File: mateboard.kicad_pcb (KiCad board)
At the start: 6 copper layers, 70 x 50 mm, 178 parts, among them IC1 OSD335x, IC2 SN74LVC2G241DCUR, IC3 NAND_4GB, IC4 WL1835MODGBMOCT, J1 IO1, J10 TEST_1P, J11 TEST_1P, J12 ANT2, J13 TEST_1P, J14 TEST_1P, J15 VDDS_PLL, J16 VDDS_DDR, J17 VDD_MPU, J18 VDD_CORE, J2 IO2, J3 GS2, J4 ANT2, J5 TEST_1P, J6 TEST_1P, J7 TEST_1P, J8 TEST_1P, J9 TEST_1P, Q1 BSS138, Q2 BSS138, U1 AP2112K-3.3TRG1, U10 TXS0108, U11 TXS0108, U2 AP2112K-1.8TRG1, U3 TL1963A-33DCQR, U4 24LC32AT-I, U5 TPS2065CDGN, U6 TPD4S012, U7 TPD4S012, U8 SN74LVC1G06DCK, U9 74LVC1G07DCK, X1 NZ2520SB-32.768KHZ-NSA3534C, Y1 24MHz, Y2 32.768kHz

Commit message: footprint check
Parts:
- U5: footprint Housings_SSOP:VSSOP-8_2.3x2mm_Pitch0.5mm -> Housings_SSOP:MSOP-8-1EP_3x3mm_Pitch0.65mm
- moved J11 13.5 mm to (65.0, 66.0)
- moved J8 11.5 mm to (63.0, 63.0)
- moved J10 10.0 mm to (63.0, 65.0)
- moved J2 7.67 mm to (54.0, 65.0)
- moved J1 6.03 mm to (116.0, 65.0)
- moved U5 4.51 mm to (117.5, 53.5)
- moved R6 4.29 mm to (115.0, 55.0)
- moved L2 4.00 mm to (118.4, 58.1)
- moved L3 4.00 mm to (116.4, 58.1)
- moved R8 3.98 mm to (115.0, 52.0), turned to 270 degrees
- moved C13 3.84 mm to (116.0, 49.2), turned to 180 degrees
- moved C28 0.60 mm to (89.8, 56.0)
- moved C20 0.50 mm to (101.3, 54.0)
- moved C22 0.50 mm to (99.8, 46.9)
- moved C23 0.50 mm to (83.0, 44.9)
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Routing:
- net VDD_3V3B: track 0.00 -> 7.56 mm, vias 0 -> 2

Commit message: wip routing
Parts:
- moved L2 3.17 mm to (118.4, 61.3)
- moved L3 3.17 mm to (116.4, 61.3)
- moved J2 3.00 mm to (54.0, 62.0)
- moved R23 1.20 mm to (113.2, 64.4)
- moved R25 1.20 mm to (113.2, 65.6)
- moved C10 0.53 mm to (65.5, 44.3)
- moved C3 0.50 mm to (104.5, 55.7)
- moved C9 0.50 mm to (100.9, 55.7)
- moved IC1 0.20 mm to (98.3, 70.3)
- moved R30 0.10 mm to (107.6, 85.1)
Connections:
- IC3 pad A2: (no net) -> /System-eMMC-GPIO/MMC1_DAT4
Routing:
- net VDD_3V3_WIFI: track 0.00 -> 87.7 mm, vias 0 -> 6
- net VDD_5V: track 0.00 -> 62.4 mm, vias 0 -> 7
- net VDD_3V3A: track 0.00 -> 37.4 mm, vias 0 -> 4
- net USB_DC: track 0.00 -> 26.7 mm, vias 0 -> 2
- net Net-(C6-Pad1): track 0.00 -> 19.3 mm
- net /LCD_DATA15: track 0.00 -> 15.5 mm, vias 0 -> 2
- net /VBAT: track 0.00 -> 14.6 mm, vias 0 -> 3
- net VDD_ADC: track 0.00 -> 13.0 mm, vias 0 -> 3
- net GNDD: track 0.00 -> 12.9 mm, vias 0 -> 8
- net /LCD_DATA3: track 0.00 -> 12.5 mm, vias 0 -> 2
- net /LCD_DATA2: track 0.00 -> 11.9 mm, vias 0 -> 2
- net /LCD_DATA14: track 0.00 -> 10.5 mm
- net Net-(D1-Pad1): track 0.00 -> 9.60 mm
- net /LCD_DATA11: track 0.00 -> 9.51 mm, vias 0 -> 2
- net SYS_5V: track 0.00 -> 7.48 mm
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
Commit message: wip routing
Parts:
- moved R39 15.6 mm to (95.1, 54.4), turned to 180 degrees
- moved R40 10.7 mm to (93.2, 54.4), turned to 180 degrees
- moved R38 5.22 mm to (83.5, 47.5)
- moved C26 3.00 mm to (99.5, 48.6)
- moved C22 2.90 mm to (99.7, 49.8)
- moved R36 2.20 mm to (99.2, 46.0)
- moved R37 2.20 mm to (99.2, 47.2)
- moved R44 1.20 mm to (83.5, 48.7)
- moved R45 1.20 mm to (83.5, 49.9)
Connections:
- IC3 pad A8: (no net) -> /System-eMMC-GPIO/MMC1_DAT7
- IC3 pad B7: (no net) -> /System-eMMC-GPIO/MMC1_DAT7
- IC3 pad C1: (no net) -> Net-(C25-Pad1)
- IC3 pad C3: (no net) -> /System-eMMC-GPIO/MMC1_DAT5
- IC3 pad C5: (no net) -> /System-eMMC-GPIO/MMC1_DAT6
- IC3 pad D1: (no net) -> /System-eMMC-GPIO/MMC1_DAT5
- IC3 pad D2: (no net) -> /System-eMMC-GPIO/MMC1_DAT5
- IC3 pad D3: (no net) -> GNDD
- IC3 pad D4: (no net) -> /System-eMMC-GPIO/MMC1_DAT6
- IC3 pad E1: (no net) -> GNDD
- IC3 pad E2: (no net) -> GNDD
- IC3 pad E3: (no net) -> /System-eMMC-GPIO/MMC1_DAT6
- IC3 pad F2: (no net) -> /System-eMMC-GPIO/MMC1_DAT6
- IC3 pad G1: (no net) -> /System-eMMC-GPIO/MMC1_DAT6
- IC3 pad M7: (no net) -> /System-eMMC-GPIO/MMC1_CLK
- IC3 pad N6: (no net) -> /System-eMMC-GPIO/MMC1_CMD
- IC3 pad N7: (no net) -> /System-eMMC-GPIO/MMC1_CMD
- IC3 pad N8: (no net) -> /System-eMMC-GPIO/MMC1_CLK
- IC3 pad P2: (no net) -> GNDD
- IC3 pad P8: (no net) -> /System-eMMC-GPIO/MMC1_CMD
- IC3 pad P9: (no net) -> /System-eMMC-GPIO/MMC1_CLK
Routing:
- net VDD_3V3B: track 11.5 -> 32.6 mm, vias 2 -> 3
- net USB_DC: track 26.7 -> 47.1 mm, vias 2 -> 3
- net GNDD: track 12.9 -> 29.2 mm, vias 8 -> 12
- net /System-eMMC-GPIO/eMMC_RSTn: track 0.00 -> 10.7 mm, vias 0 -> 2
- net /System-eMMC-GPIO/MMC1_DAT6: track 0.00 -> 8.83 mm
- net VDD_5V: track 62.4 -> 71.0 mm
- net /System-eMMC-GPIO/MMC1_DAT5: track 0.00 -> 7.50 mm
- net /System-eMMC-GPIO/MMC1_CLK: track 0.00 -> 6.38 mm
- net /System-eMMC-GPIO/MMC1_CMD: track 0.00 -> 6.09 mm
- net Net-(C25-Pad1): track 0.00 -> 5.54 mm
- net /System-eMMC-GPIO/MMC1_DAT7: track 0.00 -> 5.51 mm
- net SYS_5V: track 7.48 -> 12.1 mm
- net /System-eMMC-GPIO/MMC1_DAT1: track 0.00 -> 4.47 mm
- net /System-eMMC-GPIO/MMC1_DAT2: track 0.00 -> 4.41 mm
- net /USB-UART-WL-BT-GPIO/USB1_PWR: track 7.04 -> 10.7 mm
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
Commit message: wip routing
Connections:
- IC3 pad A9: (no net) -> VDD_3V3B
- IC3 pad B8: (no net) -> VDD_3V3B
- IC3 pad C7: (no net) -> VDD_3V3B
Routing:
- net SYS_5V: track 12.1 -> 63.2 mm, vias 0 -> 6
- net /System-eMMC-GPIO/MMC1_DAT2: track 4.41 -> 29.7 mm, vias 0 -> 2
- net /System-eMMC-GPIO/MMC1_DAT7: track 5.51 -> 30.8 mm, vias 0 -> 2
- net GNDD: track 29.2 -> 54.1 mm, vias 12 -> 17
- net /System-eMMC-GPIO/MMC1_DAT0: track 4.76 -> 27.4 mm, vias 0 -> 2
- net VDD_3V3B: track 32.6 -> 54.7 mm
- net /System-eMMC-GPIO/MMC1_DAT1: track 4.47 -> 25.7 mm, vias 0 -> 2
- net /System-eMMC-GPIO/MMC1_DAT3: track 6.04 -> 26.6 mm, vias 0 -> 2
- net /System-eMMC-GPIO/MMC1_DAT4: track 5.75 -> 26.0 mm, vias 0 -> 2
- net /System-eMMC-GPIO/MMC1_DAT5: track 7.50 -> 23.5 mm, vias 0 -> 2
- net Net-(C16-Pad2): track 0.00 -> 14.6 mm, vias 0 -> 2
- net /System-eMMC-GPIO/MMC1_DAT6: track 8.83 -> 22.6 mm, vias 0 -> 2
- net GNDA: track 0.00 -> 13.3 mm, vias 0 -> 3
- net Net-(IC1-PadP15): track 0.00 -> 12.3 mm, vias 0 -> 2
- net Net-(IC1-PadB12): track 0.00 -> 10.6 mm, vias 0 -> 2
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
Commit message: wip routing wifi
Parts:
- moved R34 10.5 mm to (113.2, 75.2)
- moved R50 3.70 mm to (55.5, 53.3)
- moved J16 2.77 mm to (107.3, 74.9)
- moved J15 2.67 mm to (107.3, 79.2)
- moved R52 1.14 mm to (56.7, 53.4)
- moved R53 1.14 mm to (57.9, 53.4)
- moved R54 1.14 mm to (59.1, 53.4)
- moved J17 0.45 mm to (97.0, 76.7)
- moved AE1 0.34 mm to (51.4, 73.7)
- moved C36 0.12 mm to (51.4, 71.9)
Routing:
- net GNDD: track 54.1 -> 216.6 mm, vias 17 -> 59
- net VDD_3V3B: track 54.7 -> 199.7 mm, vias 3 -> 15
- net GNDA: track 13.3 -> 73.4 mm, vias 3 -> 4
- net /USB-UART-WL-BT-GPIO/USB1_DRVVBUS: track 1.65 -> 46.2 mm, vias 0 -> 2
- net SYS_5V: track 63.2 -> 103.4 mm, vias 6 -> 7
- net /System-eMMC-GPIO/MMC1_CLK: track 6.38 -> 43.3 mm, vias 0 -> 2
- net /Wi-Fi BLE/WL_IRQ: track 0.00 -> 35.9 mm, vias 0 -> 2
- net /System-eMMC-GPIO/MMC1_CMD: track 6.09 -> 40.3 mm, vias 0 -> 2
- net /Power Management/LDO_PGOOD: track 0.00 -> 33.5 mm, vias 0 -> 2
- net VDD_1V8_WIFI: track 0.00 -> 26.6 mm
- net VDD_3V3A: track 38.8 -> 62.5 mm, vias 4 -> 6
- net Net-(IC1-PadC6): track 0.00 -> 20.5 mm, vias 0 -> 2
- net /Power Management/PMIC_PGOOD: track 0.00 -> 20.3 mm, vias 0 -> 2
- net /Wi-Fi BLE/WL_SDIO_D3: track 0.00 -> 18.8 mm, vias 0 -> 2
- net /USB-UART-WL-BT-GPIO/UART0_RXD.CPU: track 0.00 -> 17.3 mm, vias 0 -> 2
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- added copper zone on Ground.Cu, net GNDD

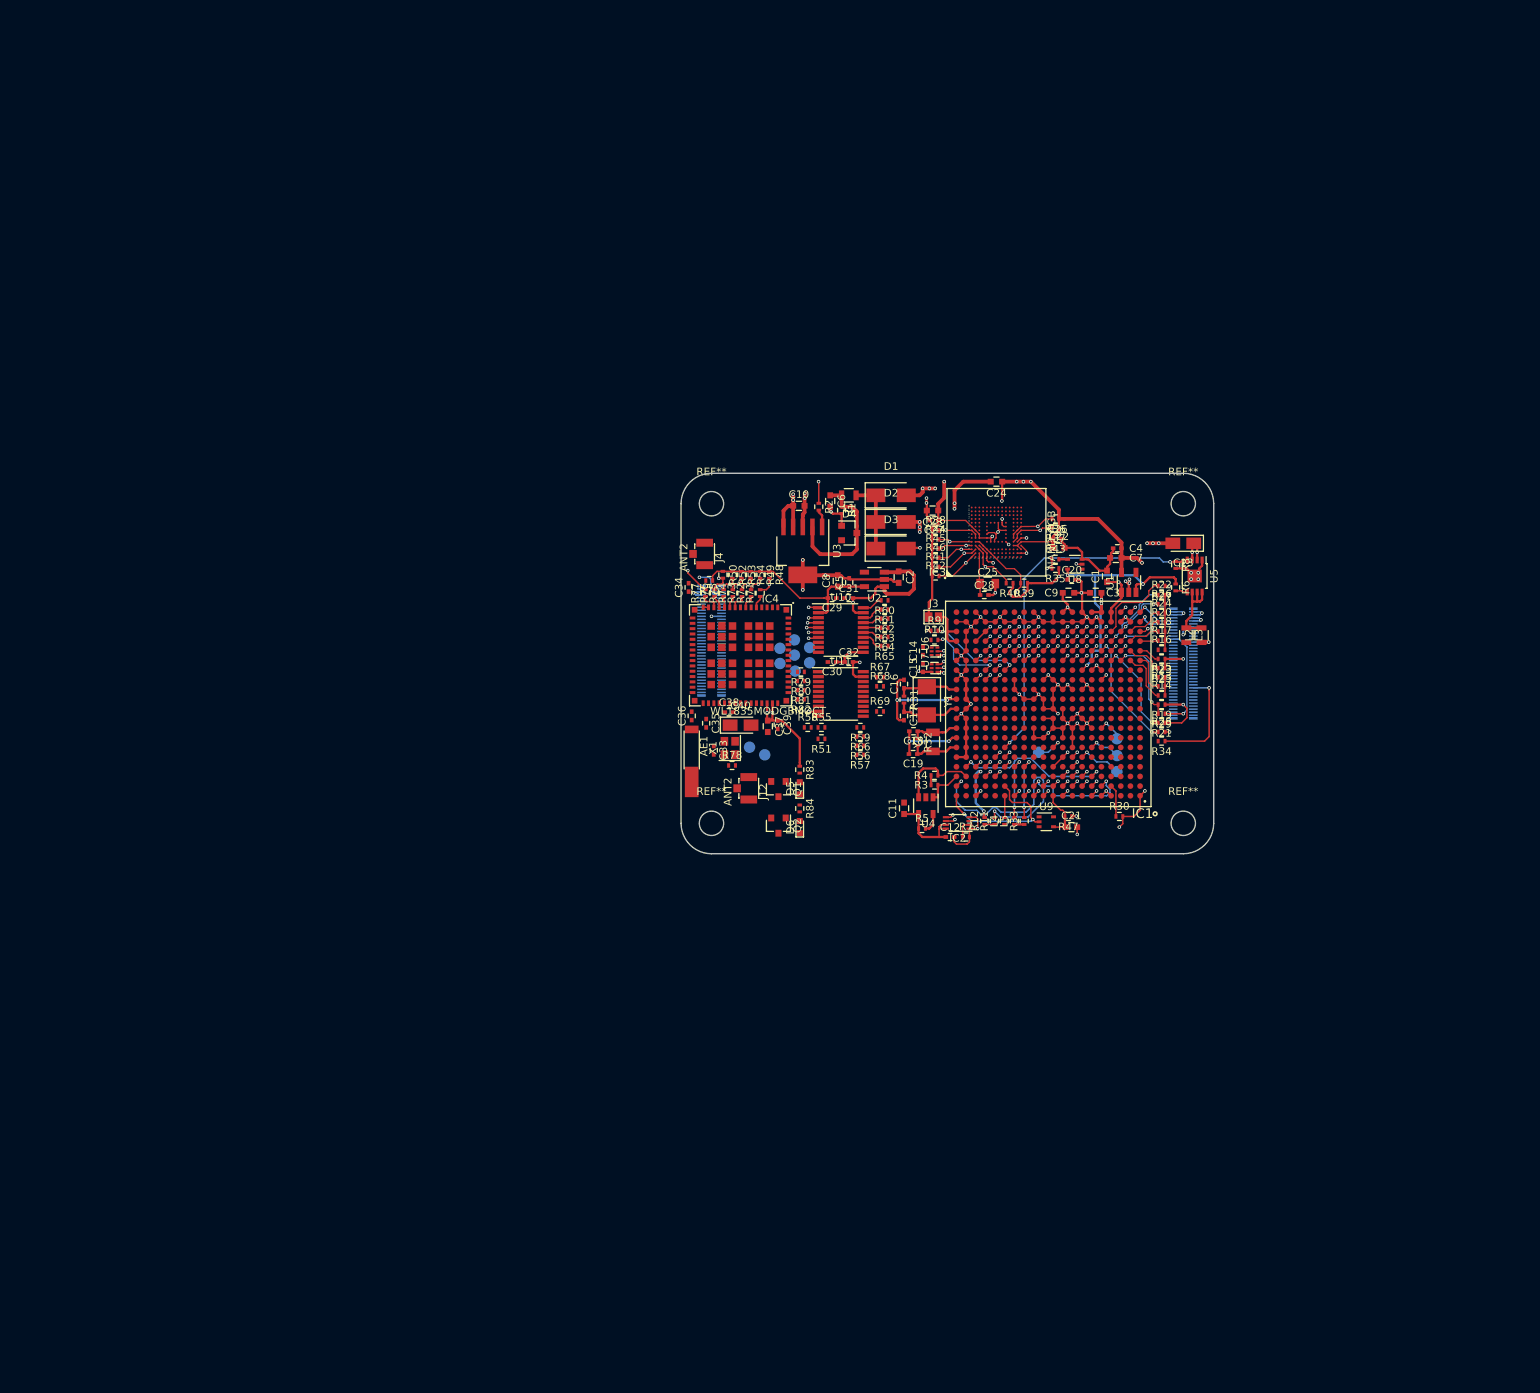
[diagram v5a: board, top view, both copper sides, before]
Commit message: connector pinout rearrangement
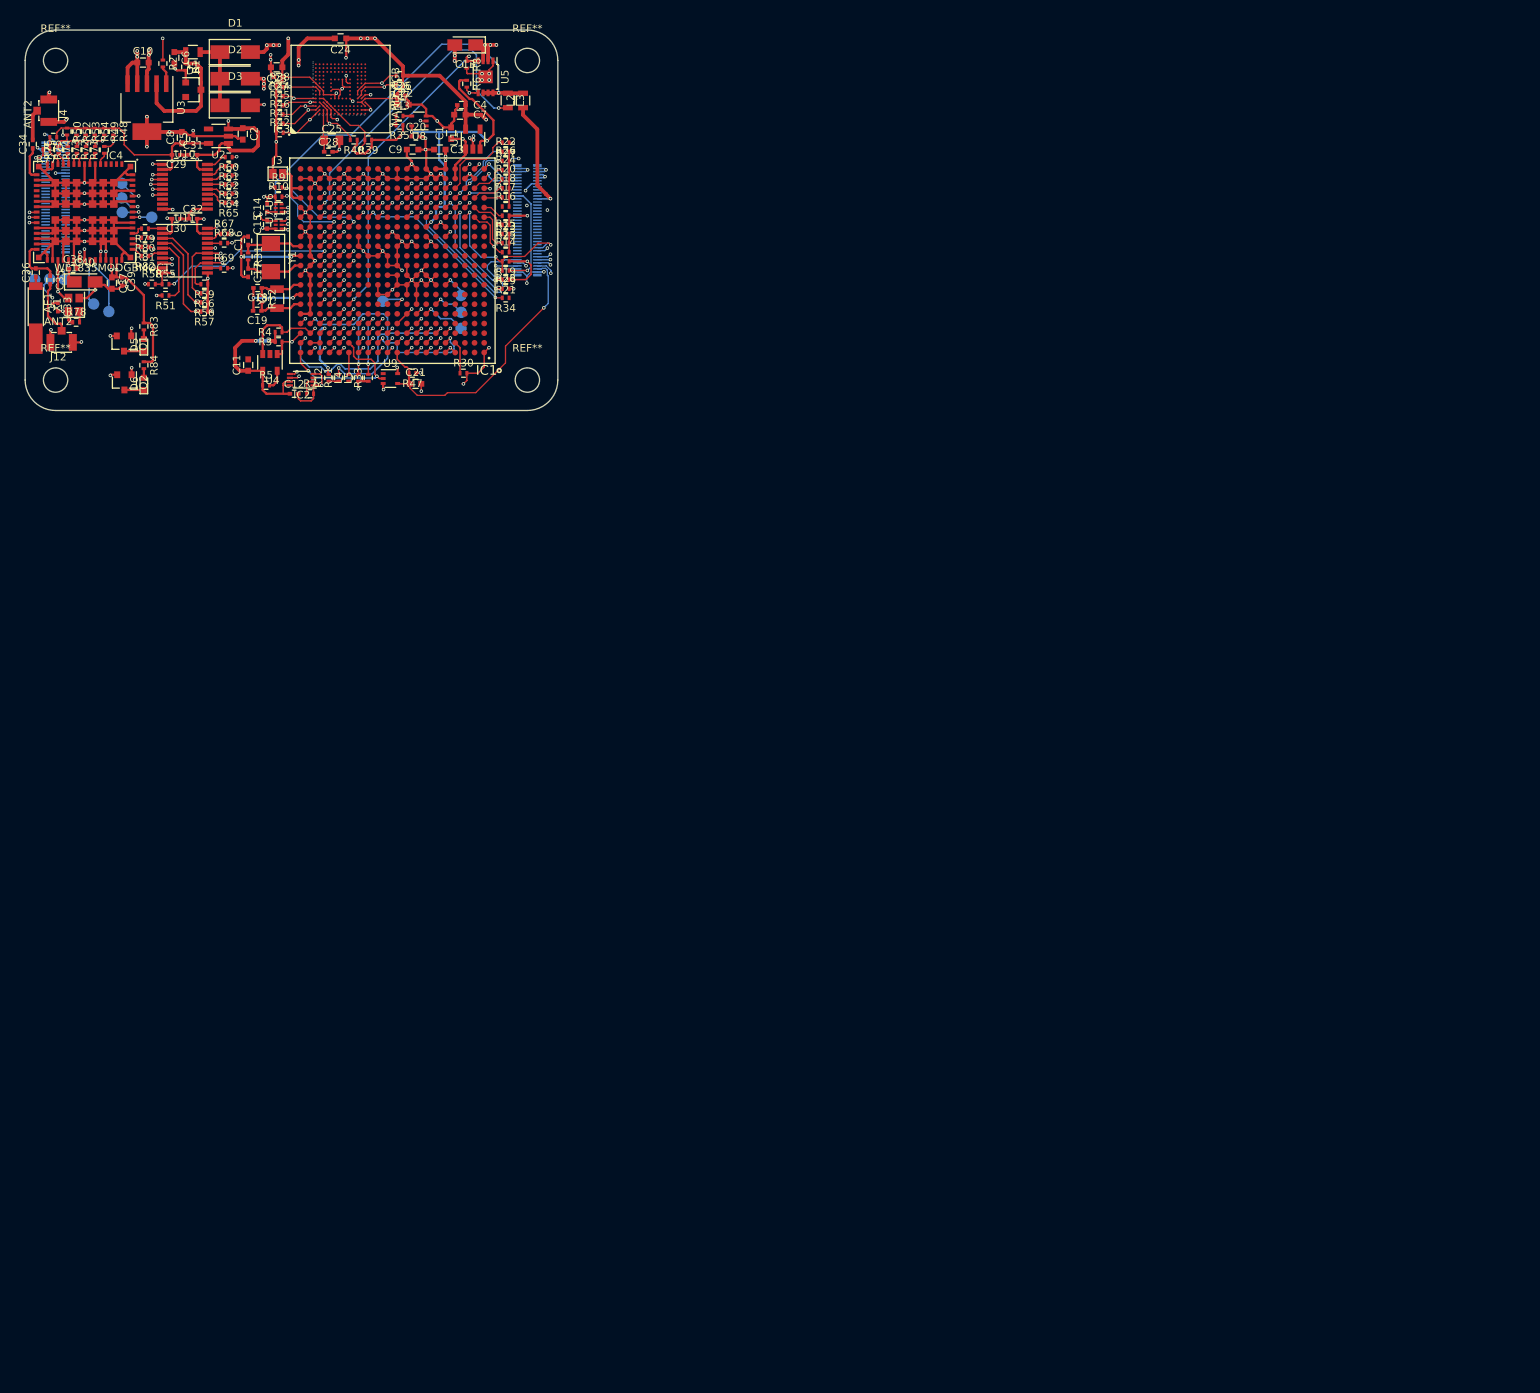
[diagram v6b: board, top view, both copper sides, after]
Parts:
- moved C13 114.9 mm to (21.6, -16.3)
- moved R6 114.3 mm to (21.8, -11.2)
- moved R8 114.0 mm to (21.8, -13.7)
- moved U5 114.0 mm to (24.3, -12.1)
- moved L2 113.5 mm to (29.2, -8.99)
- moved L3 113.5 mm to (27.2, -8.99)
- moved J8 109.3 mm to (-34.9, 14.5)
- moved J11 109.0 mm to (-31.1, 14.5)
- moved J10 108.4 mm to (-33.0, 14.5)
- moved J6 108.0 mm to (-23.5, 3.81)
- moved J12 107.6 mm to (-31.4, 22.8), turned to 180 degrees
- moved J5 106.8 mm to (-23.5, 1.91)
- moved J7 105.8 mm to (-23.4, 5.71)
- moved J17 104.6 mm to (10.8, 17.4)
- moved R77 104.4 mm to (-33.4, -2.60), turned to 180 degrees
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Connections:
- D4 pad 2: (no net) -> Net-(D4-Pad2)
- IC1 pad A2: (no net) -> Net-(IC1-PadA2)
- IC1 pad A3: (no net) -> Net-(IC1-PadA3)
- IC1 pad B1: (no net) -> Net-(IC1-PadB1)
- IC1 pad B2: (no net) -> Net-(IC1-PadB2)
- IC1 pad B3: (no net) -> Net-(IC1-PadB3)
- IC1 pad C1: (no net) -> Net-(IC1-PadC1)
- IC1 pad C10: (no net) -> Net-(IC1-PadC10)
- IC1 pad C2: (no net) -> Net-(IC1-PadC2)
- IC1 pad C3: (no net) -> Net-(IC1-PadC3)
- IC1 pad C4: (no net) -> Net-(IC1-PadC4)
- IC1 pad D1: (no net) -> Net-(IC1-PadD1)
- IC1 pad D11: (no net) -> Net-(IC1-PadD11)
- IC1 pad D2: (no net) -> Net-(IC1-PadD2)
- IC1 pad D3: (no net) -> Net-(IC1-PadD3)
- IC1 pad D4: (no net) -> Net-(IC1-PadD4)
- IC1 pad D5: (no net) -> Net-(IC1-PadD5)
- IC1 pad D6: (no net) -> Net-(IC1-PadD6)
- IC1 pad D7: (no net) -> Net-(IC1-PadD7)
- IC1 pad D9: (no net) -> Net-(IC1-PadD9)
- IC1 pad E1: (no net) -> Net-(IC1-PadE1)
- IC1 pad E10: (no net) -> Net-(IC1-PadE10)
- IC1 pad E11: (no net) -> Net-(IC1-PadE11)
- IC1 pad E12: (no net) -> Net-(IC1-PadE12)
- IC1 pad E13: (no net) -> Net-(IC1-PadE13)
- IC1 pad E14: (no net) -> Net-(IC1-PadE14)
- IC1 pad E17: (no net) -> Net-(IC1-PadE17)
- IC1 pad E18: (no net) -> Net-(IC1-PadE18)
- IC1 pad E2: (no net) -> Net-(IC1-PadE2)
- IC1 pad E3: (no net) -> Net-(IC1-PadE3)
- IC1 pad E4: (no net) -> Net-(IC1-PadE4)
- IC1 pad E5: (no net) -> Net-(IC1-PadE5)
- IC1 pad E6: (no net) -> Net-(IC1-PadE6)
- IC1 pad F1: (no net) -> Net-(IC1-PadF1)
- IC1 pad F11: (no net) -> Net-(IC1-PadF11)
- IC1 pad F12: (no net) -> Net-(IC1-PadF12)
- IC1 pad F13: (no net) -> Net-(IC1-PadF13)
- IC1 pad F14: (no net) -> Net-(IC1-PadF14)
- IC1 pad F16: (no net) -> Net-(IC1-PadF16)
- IC1 pad F2: (no net) -> Net-(IC1-PadF2)
- IC1 pad F3: (no net) -> Net-(IC1-PadF3)
- IC1 pad F4: (no net) -> Net-(IC1-PadF4)
- IC1 pad F5: (no net) -> Net-(IC1-PadF5)
- IC1 pad F7: (no net) -> Net-(IC1-PadF7)
- IC1 pad F9: (no net) -> Net-(IC1-PadF9)
- IC1 pad G1: (no net) -> Net-(IC1-PadG1)
- IC1 pad G10: (no net) -> Net-(IC1-PadG10)
- IC1 pad G13: (no net) -> Net-(IC1-PadG13)
- IC1 pad G14: (no net) -> Net-(IC1-PadG14)
- IC1 pad G2: (no net) -> Net-(IC1-PadG2)
- IC1 pad G3: (no net) -> Net-(IC1-PadG3)
- IC1 pad G4: (no net) -> Net-(IC1-PadG4)
- IC1 pad G5: (no net) -> Net-(IC1-PadG5)
- IC1 pad G6: (no net) -> Net-(IC1-PadG6)
- IC1 pad G7: (no net) -> Net-(IC1-PadG7)
- IC1 pad H1: (no net) -> Net-(IC1-PadH1)
- IC1 pad H11: (no net) -> Net-(IC1-PadH11)
- IC1 pad H13: (no net) -> Net-(IC1-PadH13)
- IC1 pad H14: (no net) -> Net-(IC1-PadH14)
- IC1 pad H15: (no net) -> Net-(IC1-PadH15)
- IC1 pad H17: (no net) -> Net-(IC1-PadH17)
- IC1 pad H2: (no net) -> Net-(IC1-PadH2)
- IC1 pad H3: (no net) -> Net-(IC1-PadH3)
- IC1 pad H4: (no net) -> Net-(IC1-PadH4)
- IC1 pad J1: (no net) -> Net-(IC1-PadJ1)
- IC1 pad J12: (no net) -> Net-(IC1-PadJ12)
- IC1 pad J13: (no net) -> Net-(IC1-PadJ13)
- IC1 pad J14: (no net) -> Net-(IC1-PadJ14)
- IC1 pad J15: (no net) -> Net-(IC1-PadJ15)
- IC1 pad J2: (no net) -> Net-(IC1-PadJ2)
- IC1 pad J3: (no net) -> Net-(IC1-PadJ3)
- IC1 pad J4: (no net) -> Net-(IC1-PadJ4)
- IC1 pad J5: (no net) -> Net-(IC1-PadJ5)
- IC1 pad K1: (no net) -> Net-(IC1-PadK1)
- IC1 pad K12: (no net) -> Net-(IC1-PadK12)
- IC1 pad K13: (no net) -> Net-(IC1-PadK13)
- IC1 pad K14: (no net) -> Net-(IC1-PadK14)
- IC1 pad K16: (no net) -> Net-(IC1-PadK16)
- IC1 pad K2: (no net) -> Net-(IC1-PadK2)
- IC1 pad K3: (no net) -> Net-(IC1-PadK3)
- IC1 pad K4: (no net) -> Net-(IC1-PadK4)
- IC1 pad K5: (no net) -> Net-(IC1-PadK5)
- IC1 pad K6: (no net) -> Net-(IC1-PadK6)
- IC1 pad K8: (no net) -> Net-(IC1-PadK8)
- IC1 pad L1: (no net) -> Net-(IC1-PadL1)
- IC1 pad L14: (no net) -> Net-(IC1-PadL14)
- IC1 pad L2: (no net) -> Net-(IC1-PadL2)
- IC1 pad L3: (no net) -> Net-(IC1-PadL3)
- IC1 pad L4: (no net) -> Net-(IC1-PadL4)
- IC1 pad L5: (no net) -> Net-(IC1-PadL5)
- IC1 pad L6: (no net) -> Net-(IC1-PadL6)
- IC1 pad L7: (no net) -> Net-(IC1-PadL7)
- IC1 pad L8: (no net) -> Net-(IC1-PadL8)
- IC1 pad L9: (no net) -> Net-(IC1-PadL9)
- IC1 pad M1: (no net) -> Net-(IC1-PadM1)
- IC1 pad M11: (no net) -> Net-(IC1-PadM11)
- IC1 pad M13: (no net) -> Net-(IC1-PadM13)
- IC1 pad M15: (no net) -> Net-(IC1-PadM15)
- IC1 pad M16: (no net) -> Net-(IC1-PadM16)
- IC1 pad M2: (no net) -> Net-(IC1-PadM2)
- IC1 pad M3: (no net) -> Net-(IC1-PadM3)
- IC1 pad M4: (no net) -> Net-(IC1-PadM4)
- IC1 pad M5: (no net) -> Net-(IC1-PadM5)
- IC1 pad N1: (no net) -> Net-(IC1-PadN1)
- IC1 pad N12: (no net) -> Net-(IC1-PadN12)
- IC1 pad N13: (no net) -> Net-(IC1-PadN13)
- IC1 pad N15: (no net) -> Net-(IC1-PadN15)
- IC1 pad N2: (no net) -> Net-(IC1-PadN2)
- IC1 pad N3: (no net) -> Net-(IC1-PadN3)
- IC1 pad N4: (no net) -> Net-(IC1-PadN4)
- IC1 pad N6: (no net) -> VRTC
- IC1 pad N8: (no net) -> Net-(IC1-PadN8)
- IC1 pad N9: (no net) -> Net-(IC1-PadN9)
- IC1 pad P1: (no net) -> Net-(IC1-PadP1)
- IC1 pad P10: (no net) -> Net-(IC1-PadP10)
- IC1 pad P11: (no net) -> Net-(IC1-PadP11)
- IC1 pad P12: (no net) -> Net-(IC1-PadP12)
- IC1 pad P13: (no net) -> Net-(IC1-PadP13)
- IC1 pad P14: (no net) -> Net-(IC1-PadP14)
- IC1 pad P18: (no net) -> Net-(IC1-PadP18)
- IC1 pad P2: (no net) -> Net-(IC1-PadP2)
- IC1 pad P3: (no net) -> Net-(IC1-PadP3)
- IC1 pad P4: (no net) -> Net-(IC1-PadP4)
- IC1 pad P8: (no net) -> Net-(IC1-PadP8)
- IC1 pad P9: (no net) -> Net-(IC1-PadP9)
- IC1 pad R10: (no net) -> Net-(IC1-PadR10)
- IC1 pad R11: (no net) -> Net-(IC1-PadR11)
- IC1 pad R15: (no net) -> Net-(IC1-PadR15)
- IC1 pad U11: (no net) -> Net-(IC1-PadU11)
- IC1 pad V10: (no net) -> Net-(IC1-PadV10)
- IC1 pad V11: (no net) -> Net-(IC1-PadV11)
- IC1 pad V14: /GPIO1_28 -> /GPIO1_17
- IC1 pad V17: /GPIO1_28 -> /GPIO1_27
- IC1 pad Y11: (no net) -> VDD_3V3AUX
- IC1 pad Y13: (no net) -> Net-(IC1-PadY13)
- IC1 pad Y14: (no net) -> Net-(IC1-PadY14)
- IC1 pad Y16: (no net) -> Net-(IC1-PadY16)
- IC1 pad Y17: (no net) -> Net-(IC1-PadY17)
- IC1 pad Y19: (no net) -> Net-(IC1-PadY19)
- IC1 pad Y20: (no net) -> Net-(IC1-PadY20)
- IC3 pad A1: /System-eMMC-GPIO/MMC1_DAT3 -> (no net)
- IC3 pad A2: /System-eMMC-GPIO/MMC1_DAT4 -> (no net)
- IC3 pad A8: /System-eMMC-GPIO/MMC1_DAT7 -> (no net)
- IC3 pad A9: VDD_3V3B -> (no net)
- IC3 pad B7: /System-eMMC-GPIO/MMC1_DAT7 -> (no net)
- IC3 pad B8: VDD_3V3B -> (no net)
- IC3 pad C1: Net-(C25-Pad1) -> (no net)
- IC3 pad C3: /System-eMMC-GPIO/MMC1_DAT5 -> (no net)
- IC3 pad C5: /System-eMMC-GPIO/MMC1_DAT6 -> (no net)
- IC3 pad C7: VDD_3V3B -> (no net)
- IC3 pad D1: /System-eMMC-GPIO/MMC1_DAT5 -> (no net)
- IC3 pad D2: /System-eMMC-GPIO/MMC1_DAT5 -> (no net)
- IC3 pad D3: GNDD -> (no net)
- IC3 pad D4: /System-eMMC-GPIO/MMC1_DAT6 -> (no net)
- IC3 pad E1: GNDD -> (no net)
- IC3 pad E2: GNDD -> (no net)
- IC3 pad E3: /System-eMMC-GPIO/MMC1_DAT6 -> (no net)
- IC3 pad F2: /System-eMMC-GPIO/MMC1_DAT6 -> (no net)
- IC3 pad G1: /System-eMMC-GPIO/MMC1_DAT6 -> (no net)
- IC3 pad M7: /System-eMMC-GPIO/MMC1_CLK -> (no net)
- IC3 pad N6: /System-eMMC-GPIO/MMC1_CMD -> (no net)
- IC3 pad N7: /System-eMMC-GPIO/MMC1_CMD -> (no net)
- IC3 pad N8: /System-eMMC-GPIO/MMC1_CLK -> (no net)
- IC3 pad P2: GNDD -> (no net)
- IC3 pad P8: /System-eMMC-GPIO/MMC1_CMD -> (no net)
- IC3 pad P9: /System-eMMC-GPIO/MMC1_CLK -> (no net)
- IC4 pad 2: (no net) -> Net-(IC4-Pad2)
- IC4 pad 21: (no net) -> Net-(IC4-Pad21)
- IC4 pad 22: (no net) -> Net-(IC4-Pad22)
- IC4 pad 3: (no net) -> Net-(IC4-Pad3)
- IC4 pad 4: (no net) -> Net-(IC4-Pad4)
- IC4 pad 5: (no net) -> Net-(IC4-Pad5)
- IC4 pad 62: (no net) -> Net-(IC4-Pad62)
- IC4 pad G1: GNDD -> (no net)
- IC4 pad G10: GNDD -> (no net)
- IC4 pad G11: GNDD -> (no net)
- IC4 pad G12: GNDD -> (no net)
- IC4 pad G13: GNDD -> (no net)
- IC4 pad G14: GNDD -> (no net)
- IC4 pad G15: GNDD -> (no net)
- IC4 pad G16: GNDD -> (no net)
- IC4 pad G17: GNDD -> (no net)
- IC4 pad G18: GNDD -> (no net)
- IC4 pad G19: GNDD -> (no net)
- IC4 pad G2: GNDD -> (no net)
- IC4 pad G20: GNDD -> (no net)
- IC4 pad G21: GNDD -> (no net)
- IC4 pad G22: GNDD -> (no net)
- IC4 pad G23: GNDD -> (no net)
- IC4 pad G24: GNDD -> (no net)
- IC4 pad G25: GNDD -> (no net)
- IC4 pad G26: GNDD -> (no net)
- IC4 pad G27: GNDD -> (no net)
- IC4 pad G28: GNDD -> (no net)
- IC4 pad G29: GNDD -> (no net)
- IC4 pad G3: GNDD -> (no net)
- IC4 pad G30: GNDD -> (no net)
- IC4 pad G31: GNDD -> (no net)
- IC4 pad G32: GNDD -> (no net)
- IC4 pad G33: GNDD -> (no net)
- IC4 pad G34: GNDD -> (no net)
- IC4 pad G35: GNDD -> (no net)
- IC4 pad G36: GNDD -> (no net)
- IC4 pad G4: GNDD -> (no net)
- IC4 pad G5: GNDD -> (no net)
- IC4 pad G6: GNDD -> (no net)
- IC4 pad G7: GNDD -> (no net)
- IC4 pad G8: GNDD -> (no net)
- IC4 pad G9: GNDD -> (no net)
- J1 pad 12: /SYS_RESETn -> /GPIO1_28
- J1 pad 27: GNDD -> /LCD_DATA15
- J1 pad 29: /UART0_RXD -> /LCD_DATA14
- J1 pad 31: /UART0_TXD -> /LCD_DATA13
- J1 pad 33: /UART1_RXD -> /LCD_DATA12
- J1 pad 35: /UART1_TXD -> /LCD_DATA11
- J1 pad 37: /UART2_TXD -> /LCD_DATA10
- J1 pad 39: /UART2_RXD -> /LCD_DATA9
- J1 pad 41: /UART4_TXD -> /LCD_DATA8
- J1 pad 43: /UART4_RXD -> /LCD_DATA7
- J1 pad 45: /GPIO2_0 -> /LCD_DATA6
- J1 pad 47: /GPIO1_25 -> /LCD_DATA5
- J1 pad 49: /GPIO1_29 -> /LCD_DATA4
- J1 pad 51: /GPIO1_16 -> /LCD_DATA3
- J1 pad 53: /GPIO1_15 -> /LCD_DATA2
- J1 pad 55: /GPIO1_13 -> /LCD_DATA1
- J1 pad 57: /GPIO1_14 -> /LCD_DATA0
- J1 pad 59: /GPIO1_12 -> /LCD_HSYNC
- J1 pad 61: /GPIO0_27 -> /LCD_VSYNC
- J1 pad 63: /GPIO0_26 -> /LCD_PCLK
- J1 pad 65: /GPIO2_1 -> /LCD_DE
- J1 pad 67: /GPIO1_28 -> /SYS_RESETn
- J2 pad 18: GNDD -> /GPIO1_27
- J2 pad 19: /LCD_DE -> GNDD
- J2 pad 21: /LCD_PCLK -> GNDD
- J2 pad 23: /LCD_VSYNC -> /UART0_RXD
- J2 pad 25: /LCD_HSYNC -> /UART0_TXD
- J2 pad 27: GNDD -> /UART1_RXD
- J2 pad 29: /LCD_DATA0 -> /UART1_TXD
- J2 pad 31: /LCD_DATA1 -> /UART2_TXD
- J2 pad 33: /LCD_DATA2 -> /UART2_RXD
- J2 pad 35: /LCD_DATA3 -> /UART4_TXD
- J2 pad 37: /LCD_DATA4 -> /UART4_RXD
- J2 pad 39: /LCD_DATA5 -> /GPIO2_0
- J2 pad 41: /LCD_DATA6 -> /GPIO1_25
- J2 pad 43: /LCD_DATA7 -> /GPIO1_29
- J2 pad 45: /LCD_DATA8 -> /GPIO1_16
- J2 pad 47: /LCD_DATA9 -> /GPIO1_15
- J2 pad 49: /LCD_DATA10 -> /GPIO1_13
- J2 pad 51: /LCD_DATA11 -> /GPIO1_14
- J2 pad 53: /LCD_DATA12 -> /GPIO1_12
- J2 pad 55: /LCD_DATA13 -> /GPIO0_27
- J2 pad 56: GNDD -> /GPIO1_17
- J2 pad 57: /LCD_DATA14 -> /GPIO0_26
- J2 pad 59: /LCD_DATA15 -> /GPIO2_1
- U1 pad 4: (no net) -> Net-(U1-Pad4)
- U10 pad 12: (no net) -> Net-(U10-Pad12)
- U10 pad 13: (no net) -> Net-(U10-Pad13)
- U10 pad 8: (no net) -> Net-(U10-Pad8)
- U10 pad 9: (no net) -> Net-(U10-Pad9)
- U2 pad 4: (no net) -> Net-(U2-Pad4)
- U6 pad 3: (no net) -> Net-(U6-Pad3)
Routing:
- net GNDD: track 216.6 -> 403.6 mm, vias 59 -> 87
- net /PWR_BUT: track 0.00 -> 61.0 mm, vias 0 -> 2
- net /Wi-Fi BLE/BT_EN: track 0.00 -> 55.5 mm, vias 0 -> 3
- net /Wi-Fi BLE/WL_EN: track 0.00 -> 44.3 mm, vias 0 -> 3
- net /USB-UART-WL-BT-GPIO/USB1_PWR: track 10.7 -> 52.9 mm, vias 0 -> 2
- net Net-(IC1-PadT18): track 0.00 -> 41.1 mm, vias 0 -> 2
- net /Wi-Fi BLE/BT_HCI_TX.CPU: track 0.00 -> 41.1 mm, vias 0 -> 2
- net VDD_1V8_WIFI: track 26.6 -> 67.5 mm, vias 0 -> 4
- net VDD_3V3B: track 199.7 -> 237.4 mm, vias 15 -> 18
- net /Wi-Fi BLE/WL_SDIO_CMD.CPU: track 0.00 -> 35.9 mm, vias 0 -> 2
- net /CLKOUT2: track 1.30 -> 35.3 mm, vias 0 -> 2
- net /Wi-Fi BLE/WL_SDIO_CLK.CPU: track 0.00 -> 33.8 mm, vias 0 -> 2
- net /Wi-Fi BLE/BT_HCI_CTS.CPU: track 0.00 -> 31.5 mm, vias 0 -> 2
- net /Wi-Fi BLE/BT_HCI_RTS.CPU: track 0.00 -> 31.4 mm, vias 0 -> 2
- net /SYS_RESETn: track 6.58 -> 37.8 mm, vias 0 -> 1
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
